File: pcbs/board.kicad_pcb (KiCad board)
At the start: 2 copper layers, 166.6 x 164.6 mm, 90 parts

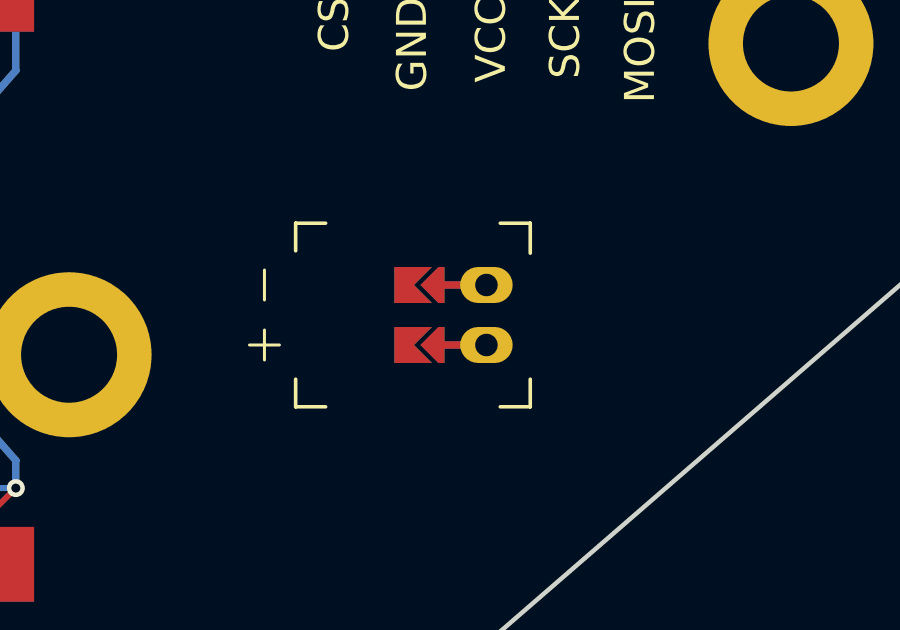
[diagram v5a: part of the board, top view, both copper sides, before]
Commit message: More comments, shift battery jst to the right
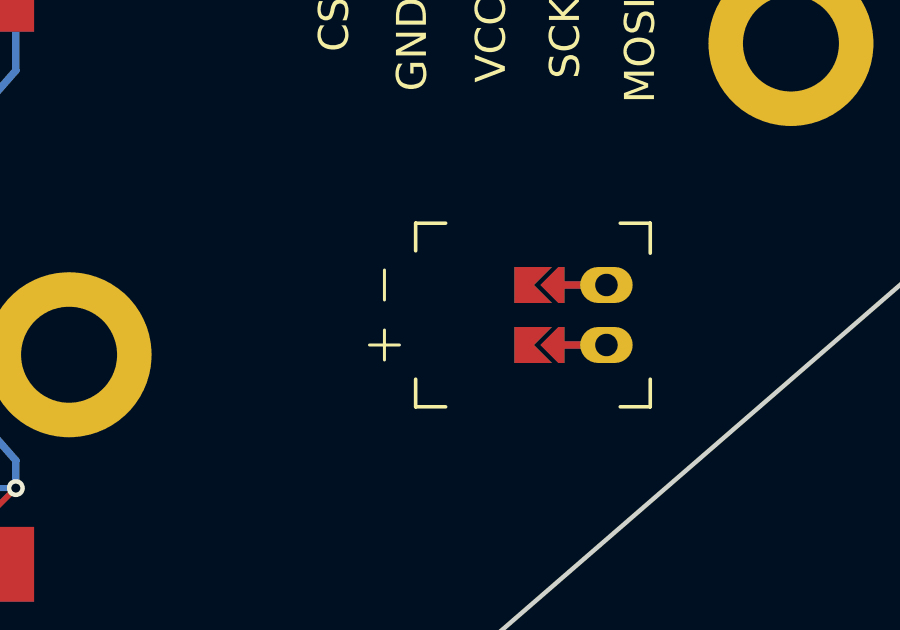
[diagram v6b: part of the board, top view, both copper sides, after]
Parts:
- moved JST1 4.00 mm to (191.4, 95.1)
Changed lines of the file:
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@@
     (footprint "ceoloide:battery_connector_jst_ph_2"
         (layer "F.Cu")
-        (at 187.4375 95.14999999999999 -90)
+        (at 191.4375 95.14999999999999 -90)
         (property "Reference" "JST1"
             (at 0 4.8 -90)
@@
         )
     )
-    (segment (start 185.6375 94.14999999999999) (end 187.4375 94.14999999999999) (width 0.25) (layer "F.Cu") (net 96))
-    (segment (start 185.6375 94.14999999999999) (end 187.4375 94.14999999999999) (width 0.25) (layer "B.Cu") (net 96))
-    (segment (start 185.6375 96.14999999999999) (end 187.4375 96.14999999999999) (width 0.25) (layer "F.Cu") (net 97))
-    (segment (start 185.6375 96.14999999999999) (end 187.4375 96.14999999999999) (width 0.25) (layer "B.Cu") (net 97))
+    (segment (start 189.6375 94.14999999999999) (end 191.4375 94.14999999999999) (width 0.25) (layer "F.Cu") (net 96))
+    (segment (start 189.6375 94.14999999999999) (end 191.4375 94.14999999999999) (width 0.25) (layer "B.Cu") (net 96))
+    (segment (start 189.6375 96.14999999999999) (end 191.4375 96.14999999999999) (width 0.25) (layer "F.Cu") (net 97))
+    (segment (start 189.6375 96.14999999999999) (end 191.4375 96.14999999999999) (width 0.25) (layer "B.Cu") (net 97))
   (footprint "ceoloide:power_switch_smd_side"
     (layer "F.Cu")

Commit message: Built previous commit
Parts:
- removed D35, D36, D37, D38: , ceoloide:diode_tht_sod123
- added RE1: , ceoloide:rotary_encoder_ec11_ec12, F.Cu at (185.0, 94.6)
- moved D34 67.0 mm to (185.0, 94.6), turned to 270 degrees
- moved PWR1 34.2 mm to (202.6, 44.0)
- moved JST1 10.5 mm to (201.6, 92.6)
- moved RST1 8.43 mm to (202.6, 65.1)
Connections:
- D34 pad 1: RW0 -> RW4
- D34 pad 2: t_col0_near -> encoder_encoder
- MCU1 pad 118: P4 -> EN2
- MCU1 pad 123: P0 -> EN1
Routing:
- net (no net): track 873.6 -> 918.1 mm
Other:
- board size 166.6 x 164.6 mm -> 171.6 x 164.6 mm
